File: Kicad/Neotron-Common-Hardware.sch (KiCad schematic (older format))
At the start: 0 parts

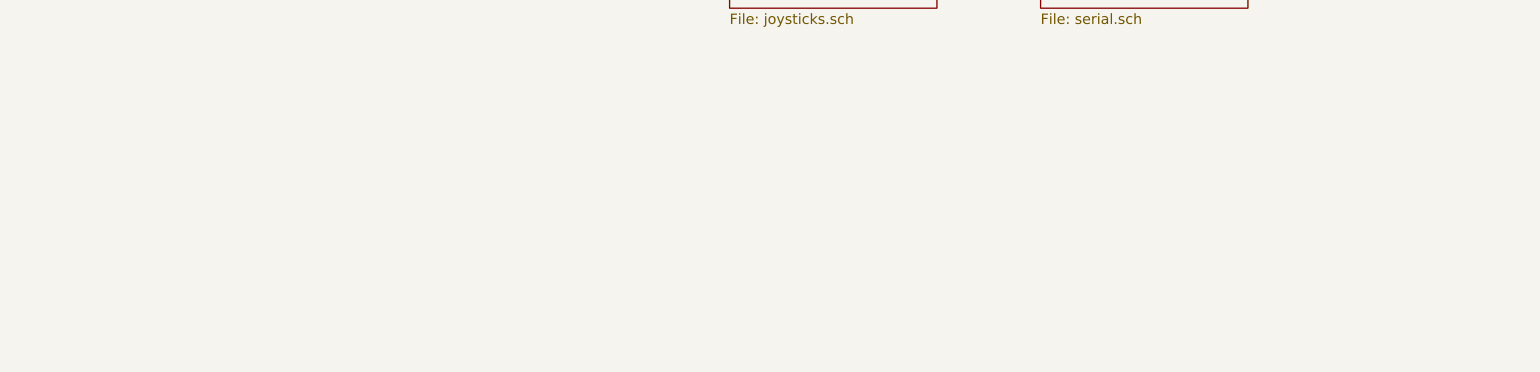
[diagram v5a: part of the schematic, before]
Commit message: Add ATX/ITX mounting holes.
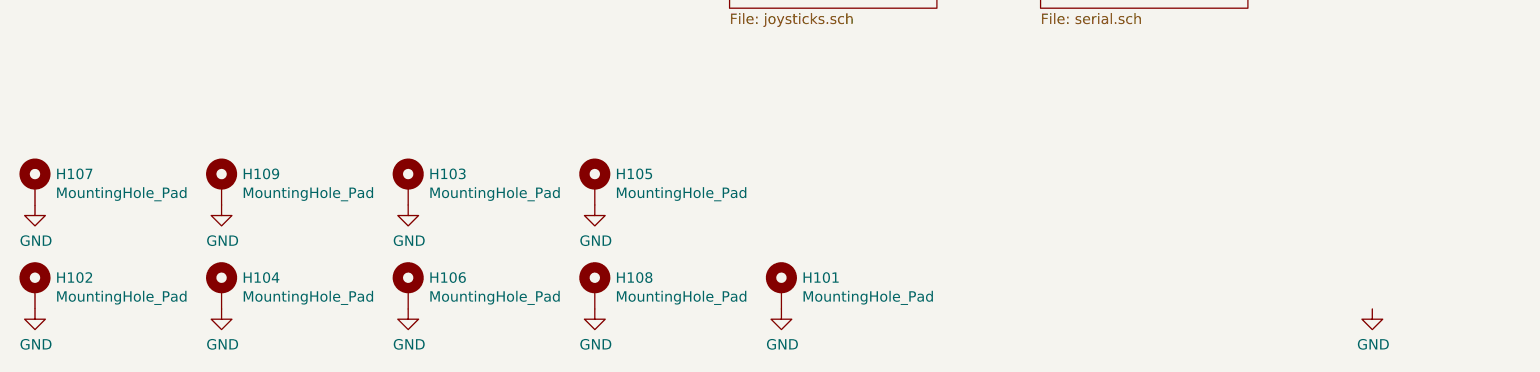
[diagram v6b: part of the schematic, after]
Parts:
- added H101, H102, H103, H104, H105, H106, H107, H108, H109: MountingHole_Pad, MountingHole:MountingHole_4.3mm_M4_Pad_Via, symbol Mechanical:MountingHole_Pad
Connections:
- net GND: now also H101.1, H102.1, H103.1, H104.1, H105.1, H106.1, H107.1, H108.1, H109.1
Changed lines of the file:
@@
 NoConn ~ 2500 3950
 NoConn ~ 2500 3650
+$Comp
+L Mechanical:MountingHole_Pad H101
+U 1 1 60B38A8B
+P 4250 7350
+F 0 "H101" H 4350 7399 50  0000 L CNN
+F 1 "MountingHole_Pad" H 4350 7308 50  0000 L CNN
+F 2 "MountingHole:MountingHole_4.3mm_M4_Pad_Via" H 4250 7350 50  0001 C CNN
+F 3 "~" H 4250 7350 50  0001 C CNN
+	1    4250 7350
+	1    0    0    -1
+$EndComp
+$Comp
+L Mechanical:MountingHole_Pad H102
+U 1 1 60B38F65
+P 650 7350
+F 0 "H102" H 750 7399 50  0000 L CNN
+F 1 "MountingHole_Pad" H 750 7308 50  0000 L CNN
+F 2 "MountingHole:MountingHole_4.3mm_M4_Pad_Via" H 650 7350 50  0001 C CNN
+F 3 "~" H 650 7350 50  0001 C CNN
+	1    650  7350
+	1    0    0    -1
+$EndComp
+$Comp
+L Mechanical:MountingHole_Pad H103
+U 1 1 60B394BF
+P 2450 6850
+F 0 "H103" H 2550 6899 50  0000 L CNN
+F 1 "MountingHole_Pad" H 2550 6808 50  0000 L CNN
+F 2 "MountingHole:MountingHole_4.3mm_M4_Pad_Via" H 2450 6850 50  0001 C CNN
+F 3 "~" H 2450 6850 50  0001 C CNN
+	1    2450 6850
+	1    0    0    -1
+$EndComp
+$Comp
+L Mechanical:MountingHole_Pad H104
+U 1 1 60B394C9
+P 1550 7350
+F 0 "H104" H 1650 7399 50  0000 L CNN
+F 1 "MountingHole_Pad" H 1650 7308 50  0000 L CNN
+F 2 "MountingHole:MountingHole_4.3mm_M4_Pad_Via" H 1550 7350 50  0001 C CNN
+F 3 "~" H 1550 7350 50  0001 C CNN
+	1    1550 7350
+	1    0    0    -1
+$EndComp
+$Comp
+L Mechanical:MountingHole_Pad H105
+U 1 1 60B39D3B
+P 3350 6850
+F 0 "H105" H 3450 6899 50  0000 L CNN
+F 1 "MountingHole_Pad" H 3450 6808 50  0000 L CNN
+F 2 "MountingHole:MountingHole_4.3mm_M4_Pad_Via" H 3350 6850 50  0001 C CNN
+F 3 "~" H 3350 6850 50  0001 C CNN
+	1    3350 6850
+	1    0    0    -1
+$EndComp
+$Comp
+L Mechanical:MountingHole_Pad H106
+U 1 1 60B39D45
+P 2450 7350
+F 0 "H106" H 2550 7399 50  0000 L CNN
+F 1 "MountingHole_Pad" H 2550 7308 50  0000 L CNN
+F 2 "MountingHole:MountingHole_4.3mm_M4_Pad_Via" H 2450 7350 50  0001 C CNN
+F 3 "~" H 2450 7350 50  0001 C CNN
+	1    2450 7350
+	1    0    0    -1
+$EndComp
+$Comp
+L Mechanical:MountingHole_Pad H108
+U 1 1 60B39D59
+P 3350 7350
+F 0 "H108" H 3450 7399 50  0000 L CNN
+F 1 "MountingHole_Pad" H 3450 7308 50  0000 L CNN
+F 2 "MountingHole:MountingHole_4.3mm_M4_Pad_Via" H 3350 7350 50  0001 C CNN
+F 3 "~" H 3350 7350 50  0001 C CNN
+	1    3350 7350
+	1    0    0    -1
+$EndComp
+$Comp
+L power:GND #PWR0104
+U 1 1 60B3BDE2
+P 650 7450
+F 0 "#PWR0104" H 650 7200 50  0001 C CNN
+F 1 "GND" H 655 7277 50  0000 C CNN
+F 2 "" H 650 7450 50  0001 C CNN
+F 3 "" H 650 7450 50  0001 C CNN
+	1    650  7450
+	1    0    0    -1
+$EndComp
+$Comp
+L power:GND #PWR0105
+U 1 1 60B3C24E
+P 1550 7450
+F 0 "#PWR0105" H 1550 7200 50  0001 C CNN
+F 1 "GND" H 1555 7277 50  0000 C CNN
+F 2 "" H 1550 7450 50  0001 C CNN
+F 3 "" H 1550 7450 50  0001 C CNN
+	1    1550 7450
+	1    0    0    -1
+$EndComp
+$Comp
+L power:GND #PWR0106
+U 1 1 60B3C465
+P 2450 7450
+F 0 "#PWR0106" H 2450 7200 50  0001 C CNN
+F 1 "GND" H 2455 7277 50  0000 C CNN
+F 2 "" H 2450 7450 50  0001 C CNN
+F 3 "" H 2450 7450 50  0001 C CNN
+	1    2450 7450
+	1    0    0    -1
+$EndComp
+$Comp
+L power:GND #PWR0107
+U 1 1 60B3C806
+P 3350 7450
+F 0 "#PWR0107" H 3350 7200 50  0001 C CNN
+F 1 "GND" H 3355 7277 50  0000 C CNN
+F 2 "" H 3350 7450 50  0001 C CNN
+F 3 "" H 3350 7450 50  0001 C CNN
+	1    3350 7450
+	1    0    0    -1
+$EndComp
+$Comp
+L power:GND #PWR0111
+U 1 1 60B3D687
+P 7100 7450
+F 0 "#PWR0111" H 7100 7200 50  0001 C CNN
+F 1 "GND" H 7105 7277 50  0000 C CNN
+F 2 "" H 7100 7450 50  0001 C CNN
+F 3 "" H 7100 7450 50  0001 C CNN
+	1    7100 7450
+	1    0    0    -1
+$EndComp
+$Comp
+L power:GND #PWR0110
+U 1 1 60B3DA51
+P 3350 6950
+F 0 "#PWR0110" H 3350 6700 50  0001 C CNN
+F 1 "GND" H 3355 6777 50  0000 C CNN
+F 2 "" H 3350 6950 50  0001 C CNN
+F 3 "" H 3350 6950 50  0001 C CNN
+	1    3350 6950
+	1    0    0    -1
+$EndComp
+$Comp
+L power:GND #PWR0109
+U 1 1 60B3DDD4
+P 2450 6950
+F 0 "#PWR0109" H 2450 6700 50  0001 C CNN
+F 1 "GND" H 2455 6777 50  0000 C CNN
+F 2 "" H 2450 6950 50  0001 C CNN
+F 3 "" H 2450 6950 50  0001 C CNN
+	1    2450 6950
+	1    0    0    -1
+$EndComp
+$Comp
+L power:GND #PWR0108
+U 1 1 60B3DFA1
+P 4250 7450
+F 0 "#PWR0108" H 4250 7200 50  0001 C CNN
+F 1 "GND" H 4255 7277 50  0000 C CNN
+F 2 "" H 4250 7450 50  0001 C CNN
+F 3 "" H 4250 7450 50  0001 C CNN
+	1    4250 7450
+	1    0    0    -1
+$EndComp
+$Comp
+L Mechanical:MountingHole_Pad H107
+U 1 1 60B4931F
+P 650 6850
+F 0 "H107" H 750 6899 50  0000 L CNN
+F 1 "MountingHole_Pad" H 750 6808 50  0000 L CNN
+F 2 "MountingHole:MountingHole_4.3mm_M4_Pad_Via" H 650 6850 50  0001 C CNN
+F 3 "~" H 650 6850 50  0001 C CNN
+	1    650  6850
+	1    0    0    -1
+$EndComp
+$Comp
+L Mechanical:MountingHole_Pad H109
+U 1 1 60B49329
+P 1550 6850
+F 0 "H109" H 1650 6899 50  0000 L CNN
+F 1 "MountingHole_Pad" H 1650 6808 50  0000 L CNN
+F 2 "MountingHole:MountingHole_4.3mm_M4_Pad_Via" H 1550 6850 50  0001 C CNN
+F 3 "~" H 1550 6850 50  0001 C CNN
+	1    1550 6850
+	1    0    0    -1
+$EndComp
+$Comp
+L power:GND #PWR0115
+U 1 1 60B49333
+P 650 6950
+F 0 "#PWR0115" H 650 6700 50  0001 C CNN
+F 1 "GND" H 655 6777 50  0000 C CNN
+F 2 "" H 650 6950 50  0001 C CNN
+F 3 "" H 650 6950 50  0001 C CNN
+	1    650  6950
+	1    0    0    -1
+$EndComp
+$Comp
+L power:GND #PWR0116
+U 1 1 60B4933D
+P 1550 6950
+F 0 "#PWR0116" H 1550 6700 50  0001 C CNN
+F 1 "GND" H 1555 6777 50  0000 C CNN
+F 2 "" H 1550 6950 50  0001 C CNN
+F 3 "" H 1550 6950 50  0001 C CNN
+	1    1550 6950
+	1    0    0    -1
+$EndComp
 $EndSCHEMATC

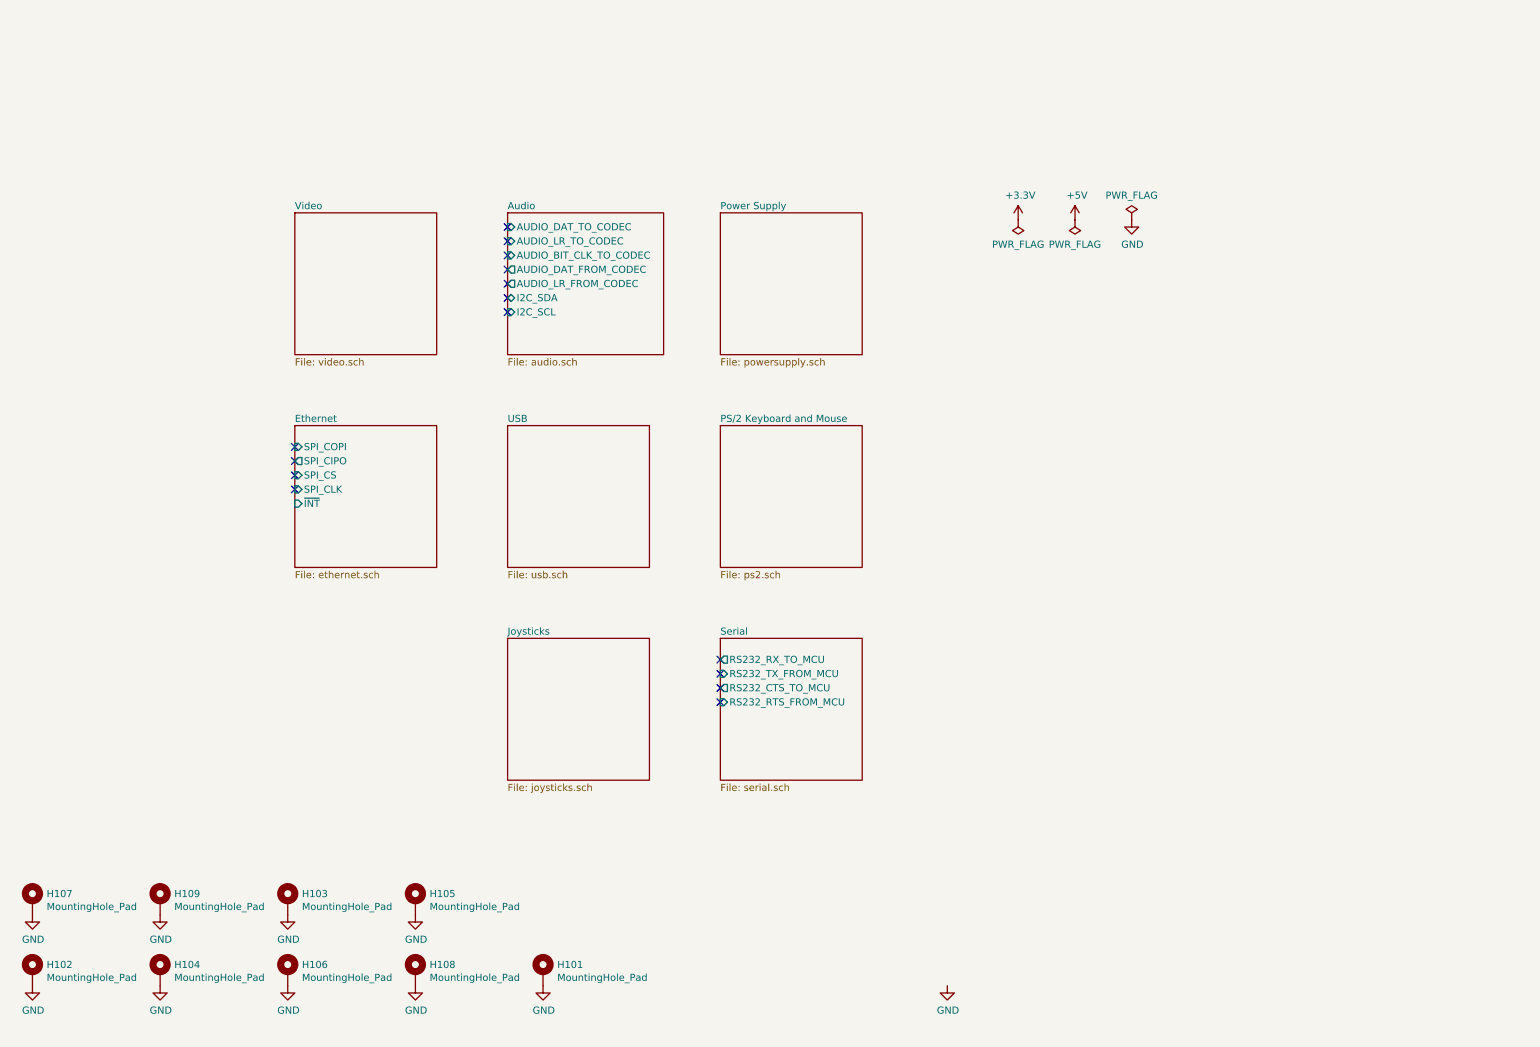
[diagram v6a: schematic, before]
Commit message: Add logos
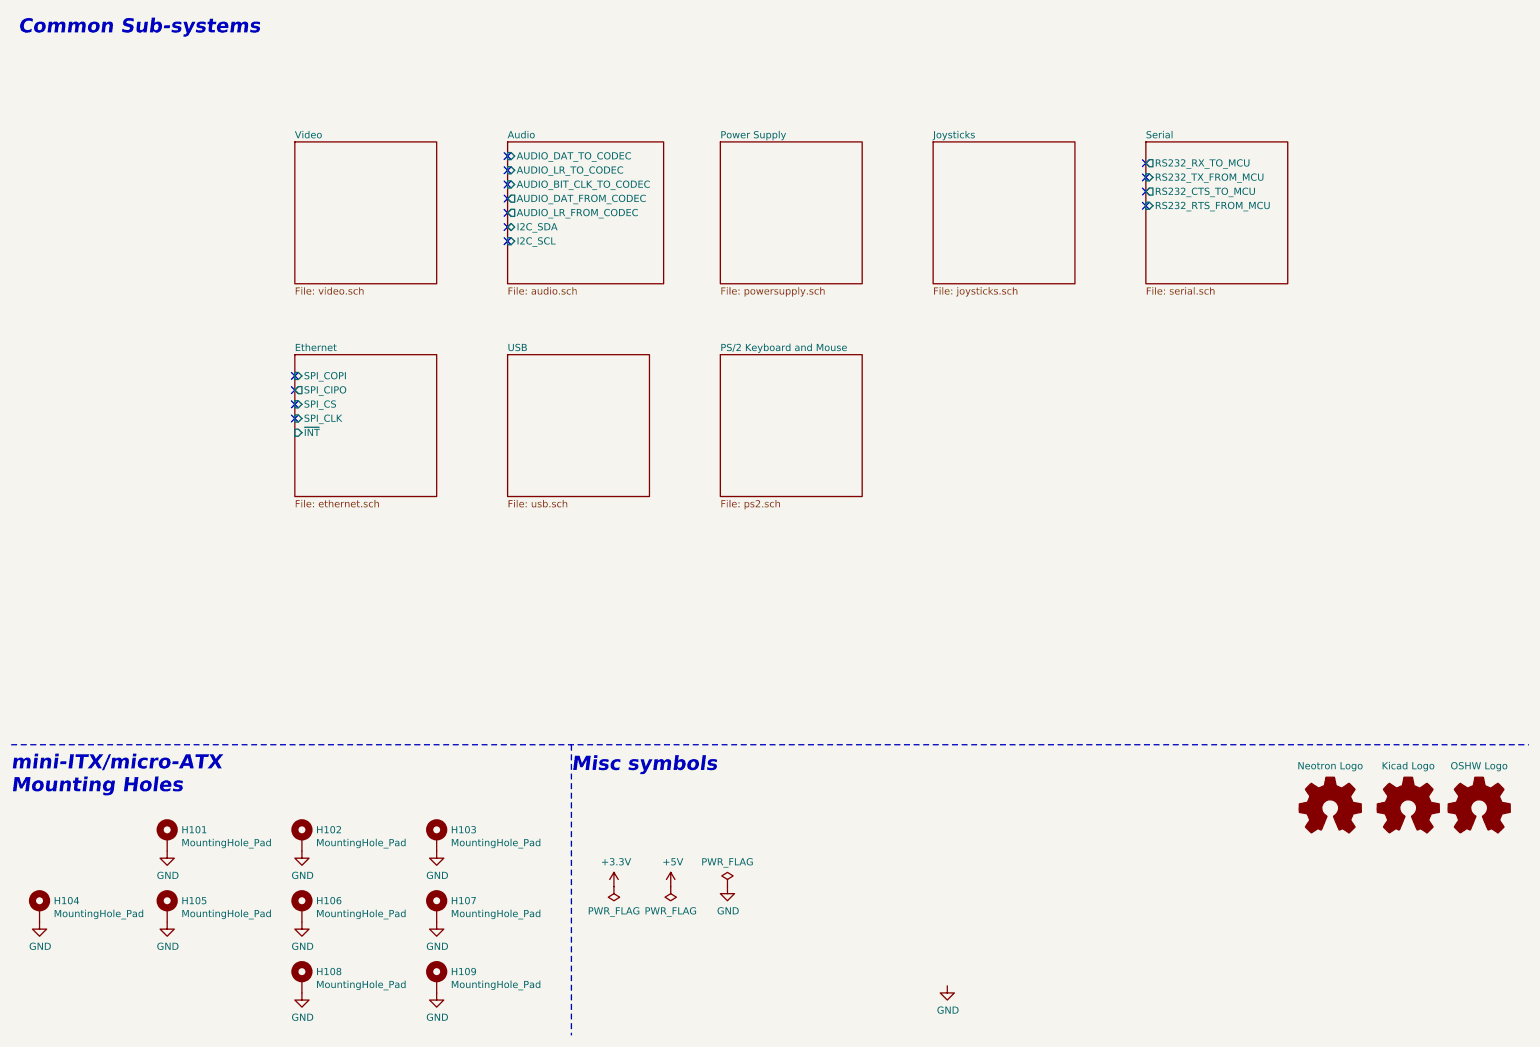
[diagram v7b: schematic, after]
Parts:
- added LOGO101: OSHW Logo, Symbol:OSHW-Logo_11.4x12mm_SilkScreen, symbol Graphic:Logo_Open_Hardware_Small
- added LOGO102: Kicad Logo, Symbol:KiCad-Logo2_12mm_SilkScreen, symbol Graphic:Logo_Open_Hardware_Small
- added LOGO103: Neotron Logo, Neotron-Common-Hardware:logo, symbol Graphic:Logo_Open_Hardware_Small
- renumbered H103 to H102, H105 to H103, H108 to H104, H102 to H105, H104 to H106, H109 to H107, H106 to H108, H107 to H109
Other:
- note added: "Common Sub-systems"
- note added: "Misc symbols"
- note added: "mini-ITX/micro-ATX\nMounting Holes"
- moved on the sheet: H101, H102, H103, H104, H105, H106, H107, H108, H109

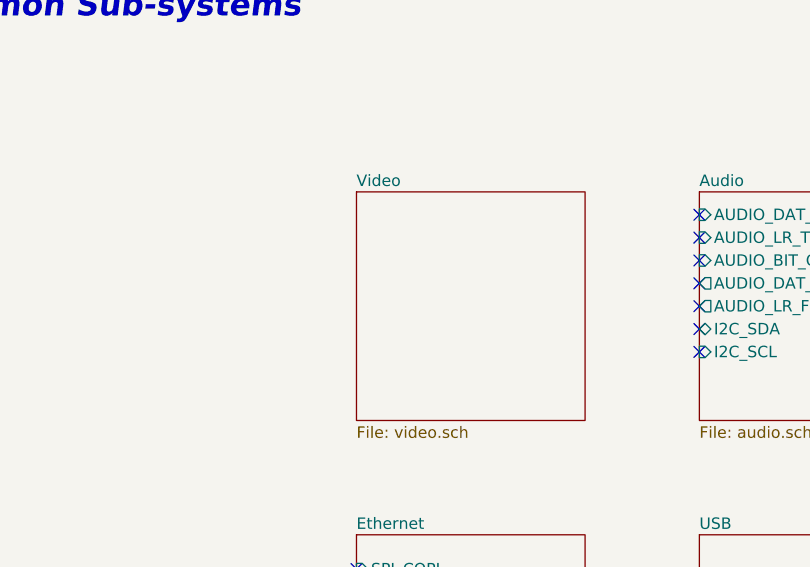
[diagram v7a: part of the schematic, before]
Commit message: Working on VGA sheet and USB sheet.
Also added courtyard and silk to stacked USB connector.
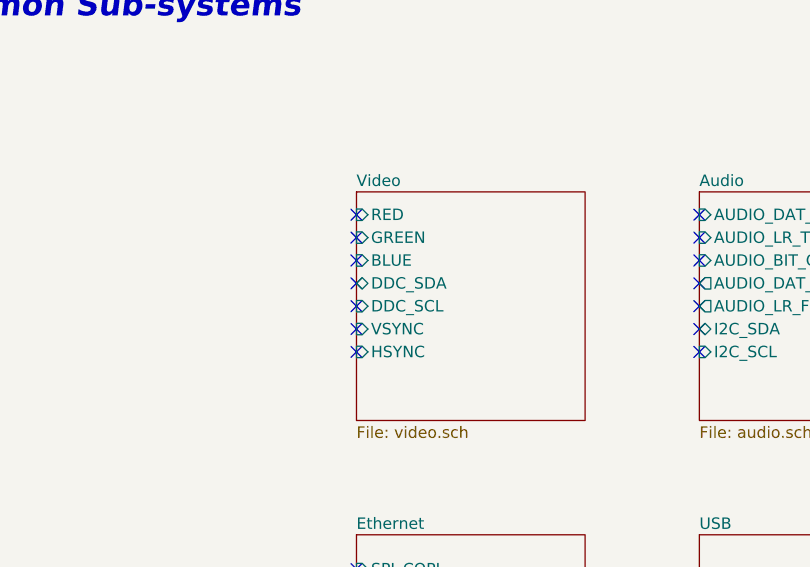
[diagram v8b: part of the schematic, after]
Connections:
- no-connect marks 15 -> 22
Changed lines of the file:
@@
 F0 "Video" 50
 F1 "video.sch" 50
+F2 "RED" I L 2500 1600 50
+F3 "GREEN" I L 2500 1700 50
+F4 "BLUE" I L 2500 1800 50
+F5 "DDC_SDA" B L 2500 1900 50
+F6 "DDC_SCL" I L 2500 2000 50
+F7 "VSYNC" I L 2500 2100 50
+F8 "HSYNC" I L 2500 2200 50
 $EndSheet
 $Sheet
@@
 	1    0    0    -1
 $EndComp
+NoConn ~ 2500 1600
+NoConn ~ 2500 1700
+NoConn ~ 2500 1800
+NoConn ~ 2500 1900
+NoConn ~ 2500 2000
+NoConn ~ 2500 2100
+NoConn ~ 2500 2200
 $EndSCHEMATC
